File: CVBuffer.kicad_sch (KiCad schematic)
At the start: 8 parts, among them P1 10K, U14 OPA333xxD

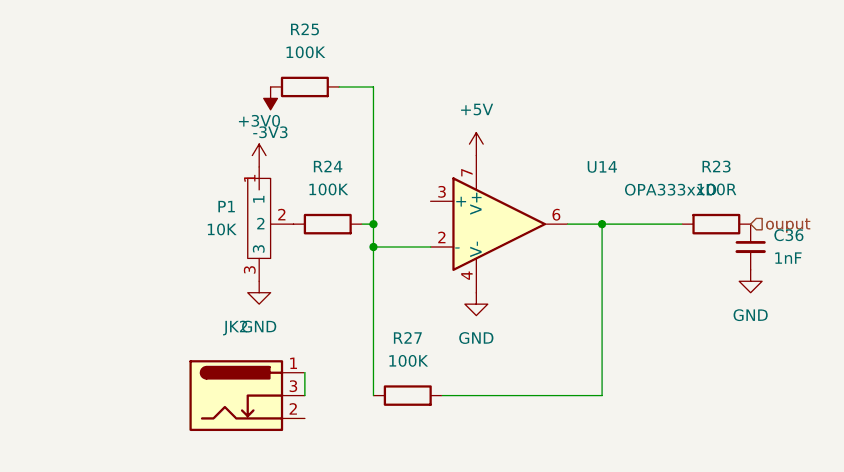
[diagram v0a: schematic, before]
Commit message: UPDATED AU88 CODEC PINS
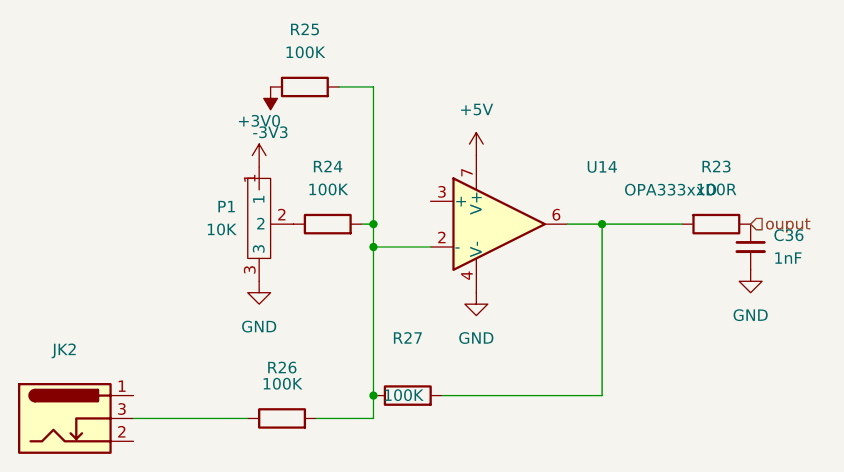
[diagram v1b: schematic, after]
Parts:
- added R26: 100K, symbol Device:R
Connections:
- net at R24.2, R25.2, R27.1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: now also R26.2
- net at JK2.1: no longer JK2.3
- new net: JK2.3, R26.1
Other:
- moved on the sheet: JK2
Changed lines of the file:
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@@
 	(paper "A4")
+	(junction
+		(at 81.28 109.22)
+		(diameter 0)
+		(color 0 0 0 0)
+	)
 	(junction
 		(at 106.68 90.17)
@@
 	(wire
 		(pts
+			(xy 74.93 111.76) (xy 81.28 111.76)
+		)
+		(stroke
+			(width 0)
+			(type default)
+		)
+	)
+	(wire
+		(pts
 			(xy 81.28 92.71) (xy 87.63 92.71)
 		)
@@
 	(wire
 		(pts
+			(xy 54.61 111.76) (xy 67.31 111.76)
+		)
+		(stroke
+			(width 0)
+			(type default)
+		)
+	)
+	(wire
+		(pts
 			(xy 106.68 90.17) (xy 115.57 90.17)
 		)
@@
 	(wire
 		(pts
+			(xy 81.28 111.76) (xy 81.28 109.22)
+		)
+		(stroke
+			(width 0)
+			(type default)
+		)
+	)
+	(wire
+		(pts
 			(xy 88.9 109.22) (xy 106.68 109.22)
 		)
@@
 		(pts
 			(xy 102.87 90.17) (xy 106.68 90.17)
-		)
-		(stroke
-			(width 0)
-			(type default)
-		)
-	)
-	(wire
-		(pts
-			(xy 73.66 109.22) (xy 73.66 106.68)
 		)
 		(stroke
@@
 		(on_board yes)
 		(dnp no)
-		(fields_autoplaced yes)
 		(property "Reference" "R27"
 			(at 85.09 102.87 90)
@@
 		)
 		(property "Value" "100K"
-			(at 85.09 105.41 90)
+			(at 84.582 109.22 90)
 			(effects
 				(font
@@
 	(symbol
 		(lib_id "esp32lib:LJE0352")
-		(at 73.66 111.76 0)
+		(at 54.61 114.3 0)
 		(unit 1)
 		(exclude_from_sim no)
@@
 		(fields_autoplaced yes)
 		(property "Reference" "JK2"
-			(at 66.04 101.6 0)
+			(at 46.99 104.14 0)
 			(effects
 				(font
@@
 		)
 		(property "Value" "~"
-			(at 66.04 104.14 0)
+			(at 46.99 106.68 0)
 			(effects
 				(font
@@
 		)
 		(property "Footprint" "customfootprints:LJE0352"
-			(at 73.66 111.76 0)
+			(at 54.61 114.3 0)
 			(effects
 				(font
@@
 		)
 		(property "Datasheet" ""
-			(at 73.66 111.76 0)
+			(at 54.61 114.3 0)
 			(effects
 				(font
@@
 		)
 		(property "Description" ""
-			(at 73.66 111.76 0)
+			(at 54.61 114.3 0)
 			(effects
 				(font
@@
 					(unit 1)
 				)
+			)
+		)
+	)
+	(symbol
+		(lib_id "Device:R")
+		(at 71.12 111.76 90)
+		(unit 1)
+		(exclude_from_sim no)
+		(in_bom yes)
+		(on_board yes)
+		(dnp no)
+		(fields_autoplaced yes)
+		(property "Reference" "R26"
+			(at 71.12 105.41 90)
+			(effects
+				(font
+					(size 1.27 1.27)
+				)
+				(justify bottom)
+			)
+		)
+		(property "Value" "100K"
+			(at 71.12 107.95 90)
+			(effects
+				(font
+					(size 1.27 1.27)
+				)
+			)
+		)
+		(property "Footprint" ""
+			(at 71.12 113.538 90)
+			(effects
+				(font
+					(size 1.27 1.27)
+				)
+				(hide yes)
+			)
+		)
+		(property "Datasheet" "~"
+			(at 71.12 111.76 0)
+			(effects
+				(font
+					(size 1.27 1.27)
+				)
+				(hide yes)
+			)
+		)
+		(property "Description" "Resistor"
+			(at 71.12 111.76 0)
+			(effects
+				(font
+					(size 1.27 1.27)
+				)
+				(hide yes)
+			)
+		)
+		(property "MFP#" "ERA-3ARB104V"
+			(at 71.12 111.76 90)
+			(effects
+				(font
+					(size 1.27 1.27)
+				)
+				(hide yes)
+			)
+		)
+		(pin "2"
+		)
+		(pin "1"
+		)
+		(instances
+			(project "esp32"
+				(path "/c4754426-a41b-4341-9d09-2e389619f3d6/29b8fac3-6ba3-4dab-8903-6b63ccf0290e"
+					(reference "R26")
+					(unit 1)
+				)

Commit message: added codec buffers
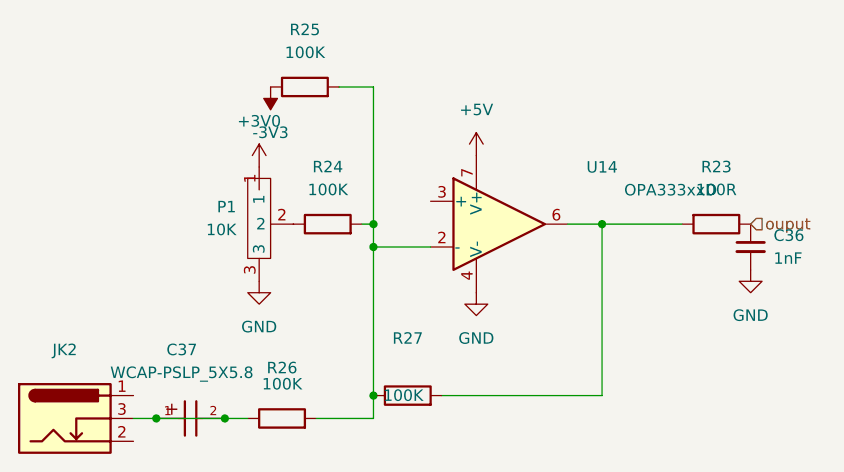
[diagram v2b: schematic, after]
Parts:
- added C37: WCAP-PSLP_5X5.8, customfootprints:WCAP-PSLP_5X5.8_DXL_, symbol esp32lib:WCAP-PSLP_5X5.8
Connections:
- net at JK2.3, R26.1: now also C37.1, C37.2
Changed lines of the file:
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@@
 	(paper "A4")
+	(junction
+		(at 64.77 111.76)
+		(diameter 0)
+		(color 0 0 0 0)
+	)
 	(junction
 		(at 81.28 109.22)
@@
 	)
 	(junction
+		(at 57.15 111.76)
+		(diameter 0)
+		(color 0 0 0 0)
+	)
+	(junction
 		(at 81.28 90.17)
 		(diameter 0)
@@
 	(wire
 		(pts
-			(xy 54.61 111.76) (xy 67.31 111.76)
+			(xy 54.61 111.76) (xy 57.15 111.76)
+		)
+		(stroke
+			(width 0)
+			(type default)
+		)
+	)
+	(wire
+		(pts
+			(xy 57.15 111.76) (xy 64.77 111.76)
 		)
 		(stroke
@@
 		(pts
 			(xy 102.87 90.17) (xy 106.68 90.17)
+		)
+		(stroke
+			(width 0)
+			(type default)
+		)
+	)
+	(wire
+		(pts
+			(xy 64.77 111.76) (xy 67.31 111.76)
 		)
 		(stroke
@@
 					(unit 1)
 				)
+			)
+		)
+	)
+	(symbol
+		(lib_id "esp32lib:WCAP-PSLP_5X5.8")
+		(at 62.23 111.76 180)
+		(unit 1)
+		(exclude_from_sim no)
+		(in_bom yes)
+		(on_board yes)
+		(dnp no)
+		(fields_autoplaced yes)
+		(property "Reference" "C37"
+			(at 59.9931 104.14 0)
+			(effects
+				(font
+					(size 1.27 1.27)
+				)
+			)
+		)
+		(property "Value" "WCAP-PSLP_5X5.8"
+			(at 59.9931 106.68 0)
+			(effects
+				(font
+					(size 1.27 1.27)
+				)
+			)
+		)
+		(property "Footprint" "customfootprints:WCAP-PSLP_5X5.8_DXL_"
+			(at 62.23 111.76 0)
+			(effects
+				(font
+					(size 1.27 1.27)
+				)
+				(justify bottom)
+				(hide yes)
+			)
+		)
+		(property "Datasheet" ""
+			(at 62.23 111.76 0)
+			(effects
+				(font
+					(size 1.27 1.27)
+				)
+				(hide yes)
+			)
+		)
+		(property "Description" ""
+			(at 62.23 111.76 0)
+			(effects
+				(font
+					(size 1.27 1.27)
+				)
+				(hide yes)
+			)
+		)
+		(pin "1"
+		)
+		(pin "2"
+		)
+		(instances
+			(project ""
+				(path "/c4754426-a41b-4341-9d09-2e389619f3d6/29b8fac3-6ba3-4dab-8903-6b63ccf0290e"
+					(reference "C37")
+					(unit 1)
+				)
